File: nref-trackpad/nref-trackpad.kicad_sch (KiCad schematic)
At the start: 11 parts, among them J1 Conn_01x06_Female, J2 Conn_01x06_Female, SW1 SW_Push, SW2 SW_Push, SW3 SW_Push, U1 PCAL6416AHF

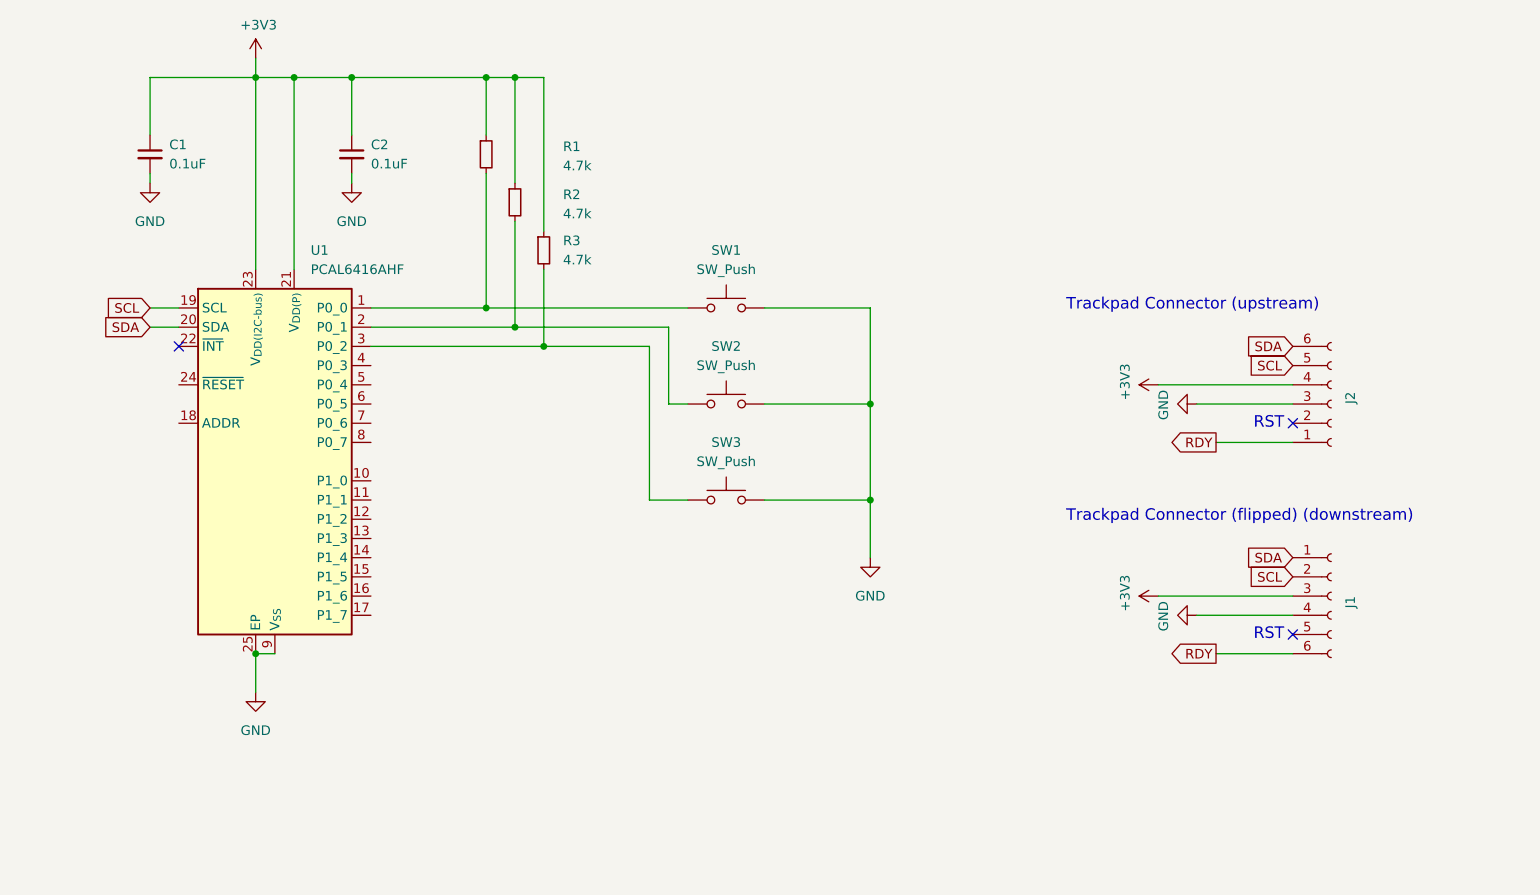
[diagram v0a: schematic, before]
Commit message: trackpad: add first button board design d-1
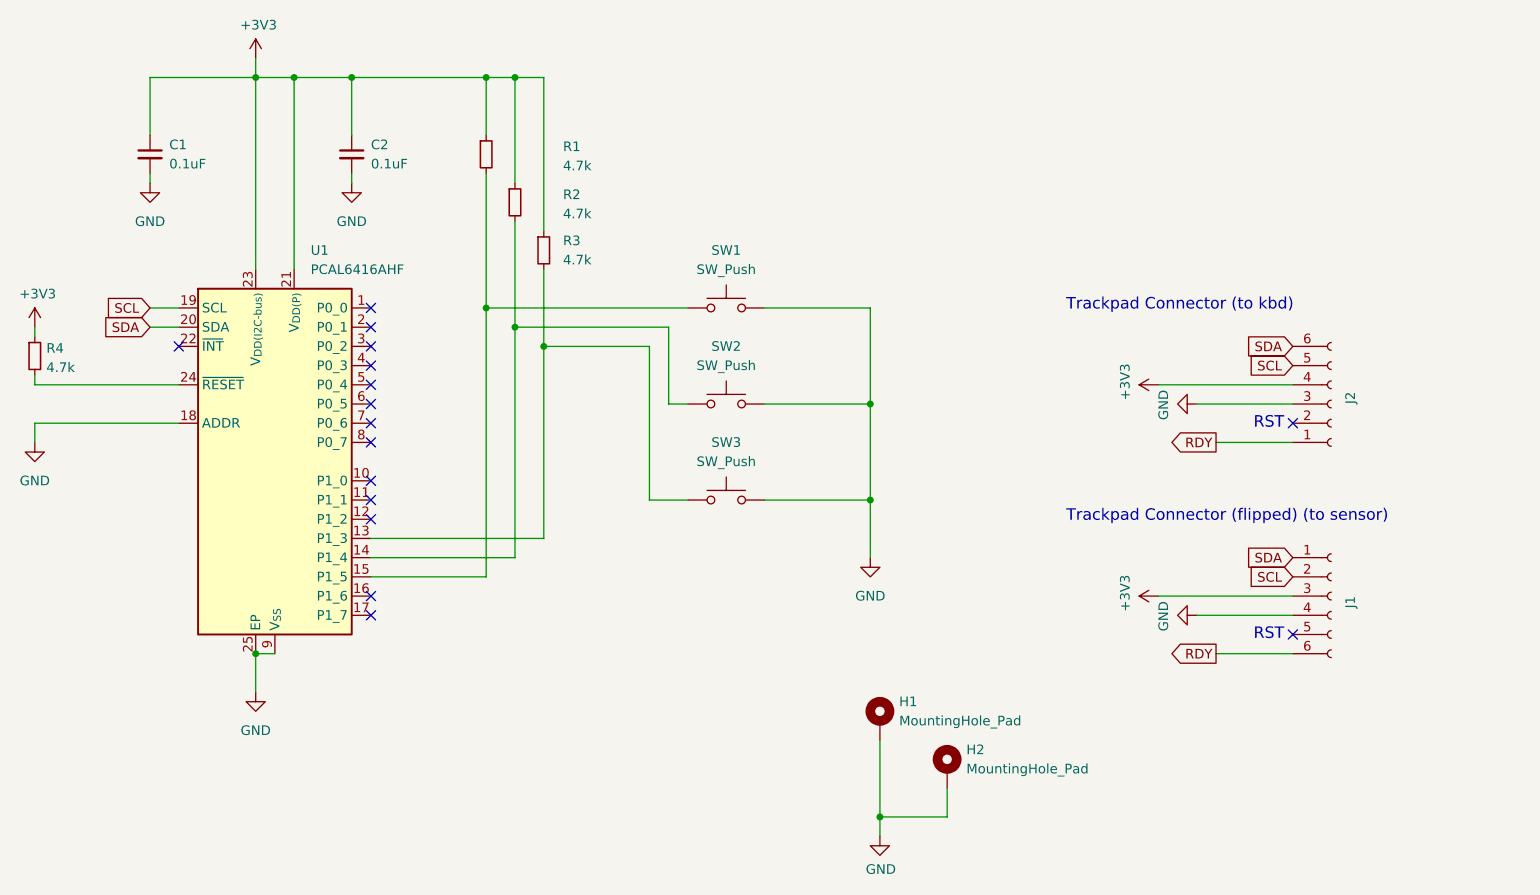
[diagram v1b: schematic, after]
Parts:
- added H1, H2: MountingHole_Pad, MountingHole:MountingHole_3.2mm_M3_Pad, symbol Mechanical:MountingHole_Pad
- added R4: 4.7k, Resistor_SMD:R_0402_1005Metric, symbol Device:R_Small
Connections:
- net +3V3: now also R4.1
- net GND: now also U1.18 (ADDR), H1.1, H2.1
- net at R1.2, SW1.1: now also U1.15 (P1_5); no longer U1.1 (P0_0)
- net at R2.2, SW2.1: now also U1.14 (P1_4); no longer U1.2 (P0_1)
- net at U1.13 (P1_3): now also R3.2, SW3.1
- net at U1.24 (~{RESET}): now also R4.2
- now unconnected: U1.3 (P0_2)
- no-connect marks 3 -> 16
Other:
- note added: "Trackpad Connector (flipped) (to sensor)"
- note added: "Trackpad Connector (to kbd)"
- note removed: "Trackpad Connector (flipped) (downstream)"
- note removed: "Trackpad Connector (upstream)"

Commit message: trackpad buttons: move left and right button further out
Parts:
- C1, C2: Manufacturer (none) -> Generic; Manufacturer_No (none) -> 0.1uF 0402
- H1, H2: Manufacturer (none) -> DNP; Manufacturer_No (none) -> DNP
- R1, R2, R3, R4: Manufacturer (none) -> Generic; Manufacturer_No (none) -> 4.7k 0402
- SW1, SW2, SW3: Manufacturer (none) -> Cherry; Manufacturer_No (none) -> ULP
- U1: Manufacturer (none) -> NXP; Manufacturer_No (none) -> PCAL6416AHF
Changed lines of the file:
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@@
+			)
+		)
+		(property "Manufacturer" "Generic"
+			(at 110.49 50.8 0)
+			(effects
+				(font
+					(size 1.27 1.27)
+				)
+				(hide yes)
+			)
+		)
+		(property "Manufacturer_No" "4.7k 0402"
+			(at 110.49 50.8 0)
+			(effects
+				(font
+					(size 1.27 1.27)
+				)
+				(hide yes)
 			)
 		)
@@
 			)
 		)
+		(property "Manufacturer" "DNP"
+			(at 162.56 125.73 0)
+			(effects
+				(font
+					(size 1.27 1.27)
+				)
+				(hide yes)
+			)
+		)
+		(property "Manufacturer_No" "DNP"
+			(at 162.56 125.73 0)
+			(effects
+				(font
+					(size 1.27 1.27)
+				)
+				(hide yes)
+			)
+		)
 		(pin "1"
 		)
@@
 			)
 		)
+		(property "Manufacturer" "Cherry"
+			(at 142.24 83.82 0)
+			(effects
+				(font
+					(size 1.27 1.27)
+				)
+				(hide yes)
+			)
+		)
+		(property "Manufacturer_No" "ULP"
+			(at 142.24 83.82 0)
+			(effects
+				(font
+					(size 1.27 1.27)
+				)
+				(hide yes)
+			)
+		)
 		(pin "1"
 		)
@@
 		)
 		(property "Description" "Resistor, small symbol"
+			(at 50.8 77.47 0)
+			(effects
+				(font
+					(size 1.27 1.27)
+				)
+				(hide yes)
+			)
+		)
+		(property "Manufacturer" "Generic"
+			(at 50.8 77.47 0)
+			(effects
+				(font
+					(size 1.27 1.27)
+				)
+				(hide yes)
+			)
+		)
+		(property "Manufacturer_No" "4.7k 0402"
 			(at 50.8 77.47 0)
 			(effects
@@
 			)
 		)
+		(property "Manufacturer" "NXP"
+			(at 82.55 91.44 0)
+			(effects
+				(font
+					(size 1.27 1.27)
+				)
+				(hide yes)
+			)
+		)
+		(property "Manufacturer_No" "PCAL6416AHF"
+			(at 82.55 91.44 0)
+			(effects
+				(font
+					(size 1.27 1.27)
+				)
+				(hide yes)
+			)
+		)
 		(pin "2"
 		)
@@
 			)
 		)
+		(property "Manufacturer" "Generic"
+			(at 118.11 63.5 0)
+			(effects
+				(font
+					(size 1.27 1.27)
+				)
+				(hide yes)
+			)
+		)
+		(property "Manufacturer_No" "4.7k 0402"
+			(at 118.11 63.5 0)
+			(effects
+				(font
+					(size 1.27 1.27)
+				)
+				(hide yes)
+			)
+		)
 		(pin "2"
 		)
@@
 			)
 		)
+		(property "Manufacturer" "Generic"
+			(at 92.71 50.8 0)
+			(effects
+				(font
+					(size 1.27 1.27)
+				)
+				(hide yes)
+			)
+		)
+		(property "Manufacturer_No" "0.1uF 0402"
+			(at 92.71 50.8 0)
+			(effects
+				(font
+					(size 1.27 1.27)
+				)
+				(hide yes)
+			)
+		)
 		(pin "2"
 		)
@@
 			)
 		)
+		(property "Manufacturer" "Cherry"
+			(at 142.24 71.12 0)
+			(effects
+				(font
+					(size 1.27 1.27)
+				)
+				(hide yes)
+			)
+		)
+		(property "Manufacturer_No" "ULP"
+			(at 142.24 71.12 0)
+			(effects
+				(font
+					(size 1.27 1.27)
+				)
+				(hide yes)
+			)
+		)
 		(pin "1"
 		)
@@
 			)
 		)
+		(property "Manufacturer" "Generic"
+			(at 114.3 57.15 0)
+			(effects
+				(font
+					(size 1.27 1.27)
+				)
+				(hide yes)
+			)
+		)
+		(property "Manufacturer_No" "4.7k 0402"
+			(at 114.3 57.15 0)
+			(effects
+				(font
+					(size 1.27 1.27)
+				)
+				(hide yes)
+			)
+		)
 		(pin "2"
 		)
@@
 			)
 		)
+		(property "Manufacturer" "Cherry"
+			(at 142.24 96.52 0)
+			(effects
+				(font
+					(size 1.27 1.27)
+				)
+				(hide yes)
+			)
+		)
+		(property "Manufacturer_No" "ULP"
+			(at 142.24 96.52 0)
+			(effects
+				(font
+					(size 1.27 1.27)
+				)
+				(hide yes)
+			)
+		)
 		(pin "1"
 		)
@@
 			)
 		)
+		(property "Manufacturer" "Generic"
+			(at 66.04 50.8 0)
+			(effects
+				(font
+					(size 1.27 1.27)
+				)
+				(hide yes)
+			)
+		)
+		(property "Manufacturer_No" "0.1uF 0402"
+			(at 66.04 50.8 0)
+			(effects
+				(font
+					(size 1.27 1.27)
+				)
+				(hide yes)
+			)
+		)
 		(pin "2"
 		)
@@
 			(at 171.45 132.08 0)
 			(effects
+				(font
+					(size 1.27 1.27)
+				)
+				(hide yes)
+			)
+		)
+		(property "Manufacturer" "DNP"
+			(at 171.45 132.08 0)
+			(effects
+				(font
+					(size 1.27 1.27)
+				)
+				(hide yes)
+			)
+		)
+		(property "Manufacturer_No" "DNP"
+			(at 171.45 132.08 0)
+			(effects
